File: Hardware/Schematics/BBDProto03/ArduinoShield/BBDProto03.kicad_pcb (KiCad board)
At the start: 2 copper layers, 91.4 x 106.7 mm, 29 parts, among them P1 Power, P11 CONN_02X08, P12 CONN_02X08, P13 CONN_02X08, P14 CONN_02X08, P15 CONN_02X08, P16 CONN_02X08, P17 CONN_02X08, P18 CONN_02X08, P2 Analog, P3 Digital, P4 Digital, P5 CONN_1, P6 CONN_1, P7 CONN_1, P8 CONN_1, P9 CONN_02X05, U1 ATTINY861-20SU, U10 CD74HC4067, U11 CD74HC4067, U12 CD74HC4067, U13 CD74HC4067, U14 CD74HC4067, U15 CD74HC4067, U16 CD74HC4067, U17 CD74HC4067, U18 CD74HC4067, U2 LTC1864, U3 MCP4822

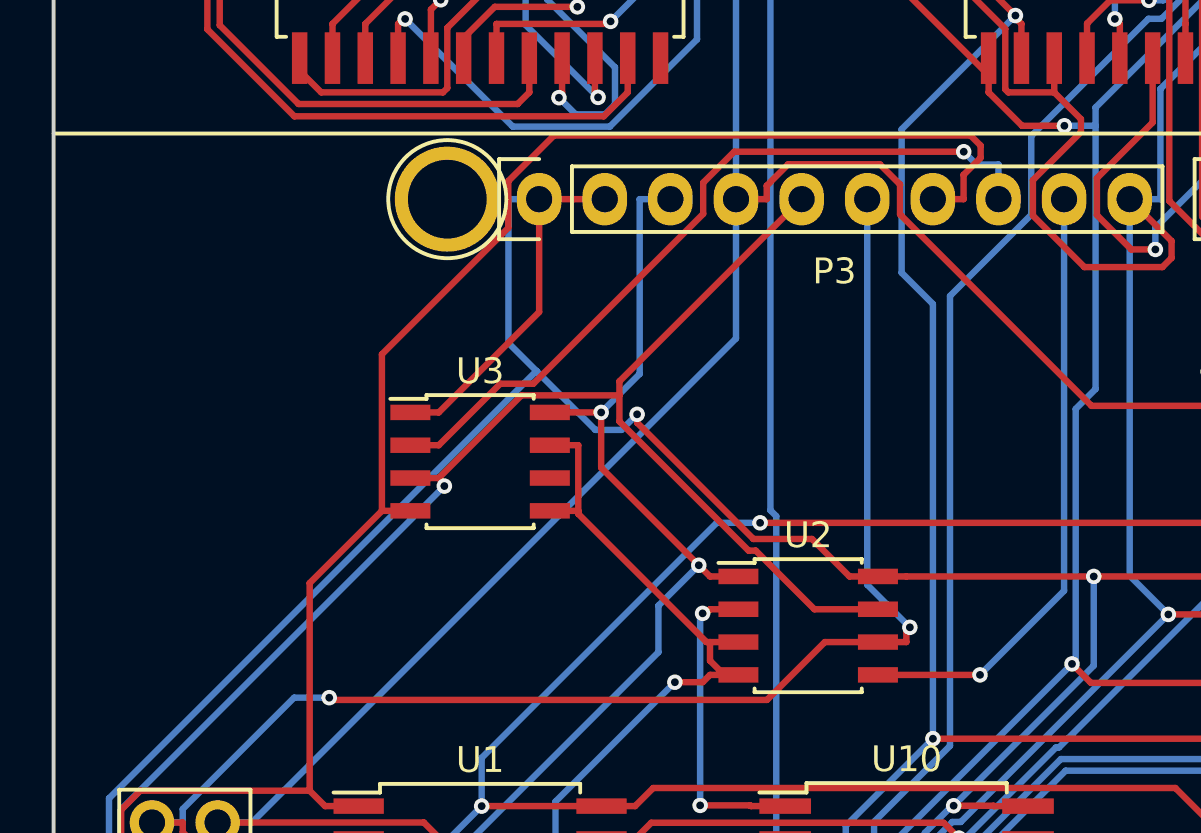
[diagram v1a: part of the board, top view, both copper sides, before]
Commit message: Added footprint associations to new components
Added footprint associations to new components: I/O transistor, reset
switch
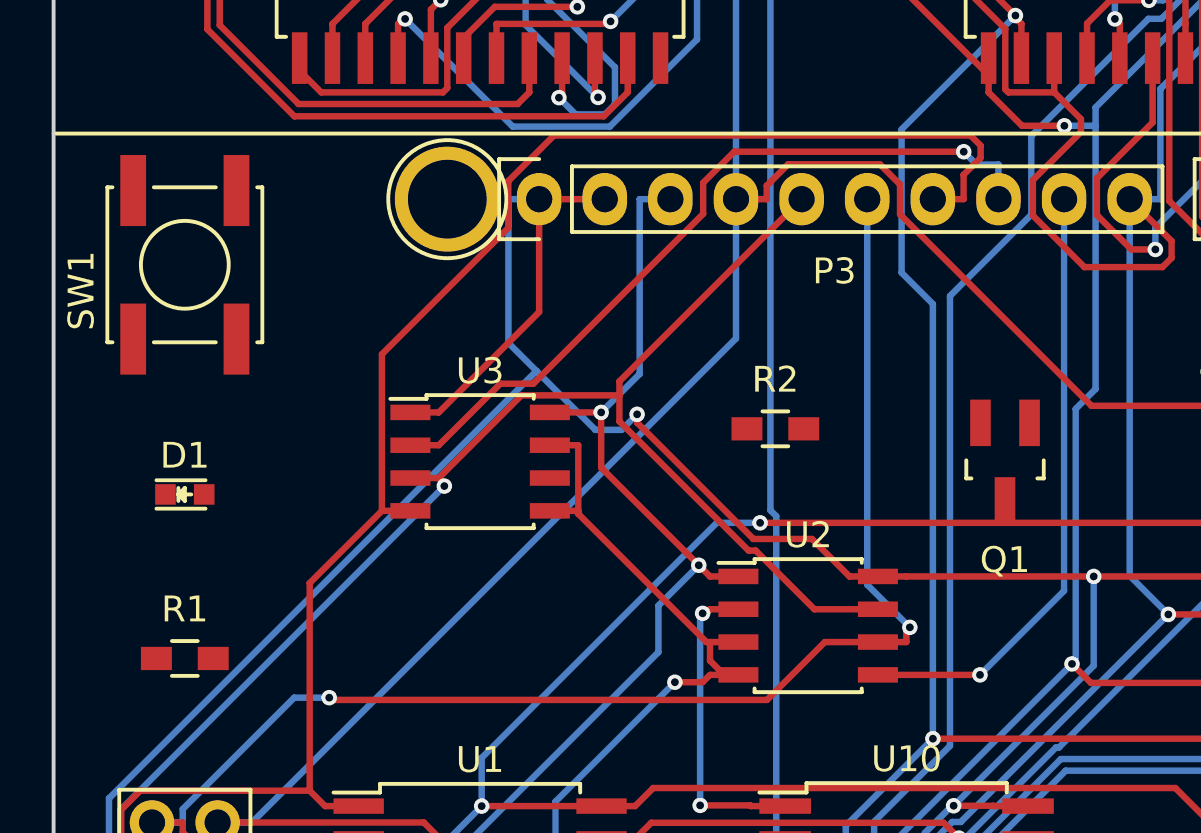
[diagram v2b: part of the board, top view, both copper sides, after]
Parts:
- added D1: LED, LEDs:LED_0603, F.Cu at (33.5, 80.6)
- added Q1: Q_NPN_BCE, TO_SOT_Packages_SMD:SOT-23_Handsoldering, F.Cu at (65.3, 79.4)
- added R1: 1k, Resistors_SMD:R_0603_HandSoldering, F.Cu at (33.5, 87.0)
- added R2: 1k, Resistors_SMD:R_0603_HandSoldering, F.Cu at (56.4, 78.1)
- added SW1: SW_PUSH, Buttons_Switches_SMD:SW_SPST_EVPBF, F.Cu at (33.5, 71.8)
- P9: value CONN_02X05 -> USBASP
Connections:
- U10 pad 15: /8 -> GND
- U11 pad 15: /8 -> GND
- U12 pad 15: /8 -> GND
- U13 pad 15: /8 -> GND
- U14 pad 15: /8 -> GND
- U15 pad 15: /8 -> GND
- U16 pad 15: /8 -> GND
- U17 pad 15: /8 -> GND
- U18 pad 15: /8 -> GND
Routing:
- net /8: track 285.0 -> 19.4 mm, vias 6 -> 0
- net GND: track 268.7 -> 534.4 mm, vias 2 -> 8

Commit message: AutoRouter rerun, new photos and fabrication files
AutoRouter rerun, new photos and fabrication files
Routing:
- net GND: track 534.4 -> 366.6 mm, vias 8 -> 3
- net Net-(D1-Pad1): track 55.3 -> 119.3 mm, vias 2 -> 0
- net /Reset: track 39.0 -> 83.5 mm
- net Net-(U1-Pad19): track 279.9 -> 237.8 mm, vias 5 -> 6
- net Net-(Q1-Pad3): track 12.2 -> 49.8 mm, vias 2 -> 0
- net Net-(U1-Pad17): track 234.9 -> 271.5 mm, vias 6 -> 3
- net Net-(U1-Pad20): track 299.8 -> 265.2 mm
- net Net-(R2-Pad2): track 0.00 -> 34.5 mm
- net /8: track 19.4 -> 52.9 mm, vias 0 -> 1
- net /+3.3V: track 291.5 -> 324.9 mm, vias 6 -> 7
- net Net-(P11-Pad12): track 50.8 -> 18.2 mm, vias 0 -> 1
- net Net-(P18-Pad6): track 40.4 -> 13.8 mm
- net Net-(P14-Pad16): track 34.5 -> 9.93 mm, vias 0 -> 1
- net Net-(R1-Pad1): track 0.00 -> 23.6 mm
- net Net-(P13-Pad5): track 48.4 -> 25.1 mm
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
